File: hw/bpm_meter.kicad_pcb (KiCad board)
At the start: 2 copper layers, 55 x 73.5 mm, 103 parts, among them J1 Conn_01x03_Pin, J901 USB_C_Receptacle_USB2.0, Q1 AO3400A, Q10 DMN2004VK, Q11 DMN2004VK, Q12 DMN2004VK, Q13 DMN2004VK, Q2 DMN2004VK, Q3 DMN2004VK, Q4 DMN2004VK, Q5 DMN2004VK, Q6 DMN2004VK, Q7 DMN2004VK, Q8 DMN2004VK, Q9 DMN2004VK, SW901 SW_MEC_5E, U1 SLS0391FR1A1GD, U2 AOZ1282CI, U3 H11L1, U4 SLS0391FR1A1GD, U5 SLS0391FR1A1GD, U901 RP2040, U902 AMS1117-3.3, U903 W25Q128JVS, Y901 Crystal_GND24_Small

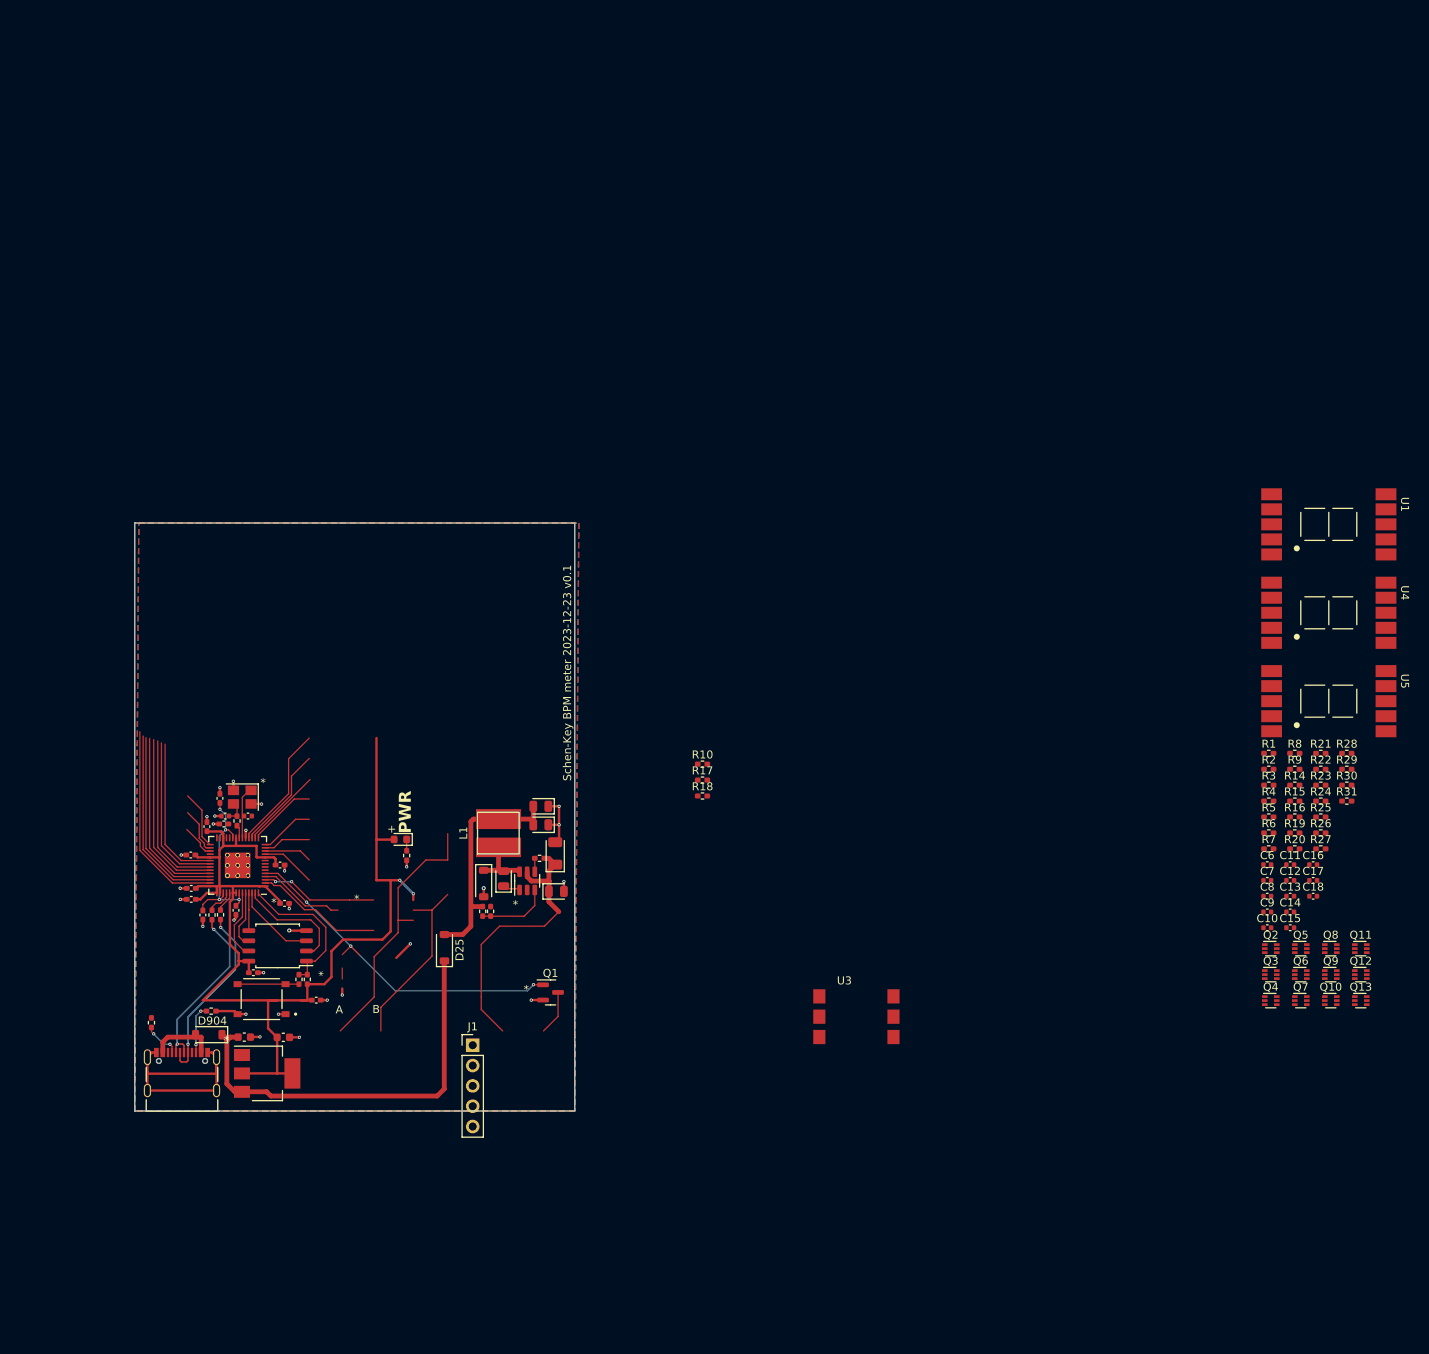
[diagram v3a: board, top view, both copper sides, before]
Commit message: Now using LP5030 LED driver
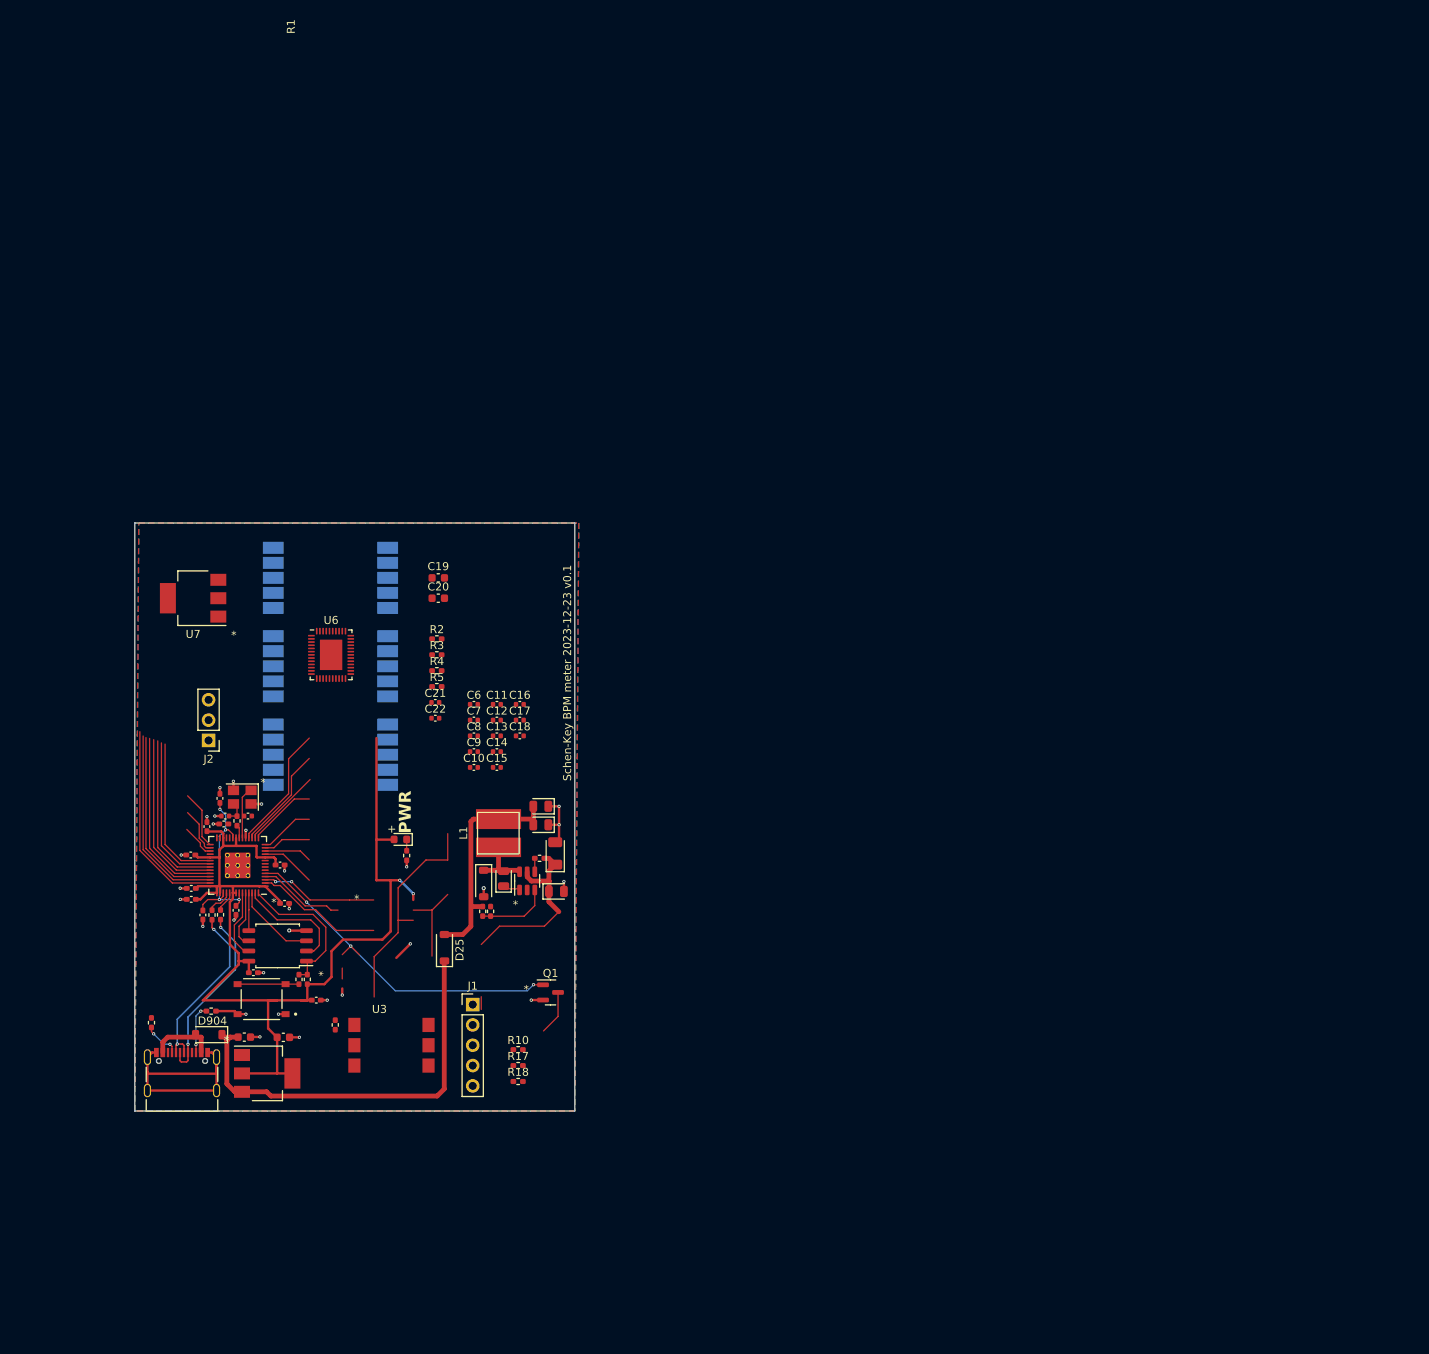
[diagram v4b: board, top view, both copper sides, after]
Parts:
- removed Q10, Q11, Q12, Q13, Q2, Q3, Q4, Q5, Q6, Q7, Q8, Q9: DMN2004VK, Package_TO_SOT_SMD:SOT-563
- removed R14, R15, R16, R19, R20, R21, R22, R23, R24, R25, R26, R27, R28, R29, R30, R31, R6, R7, R8, R9: 220, Resistor_SMD:R_0402_1005Metric_Pad0.72x0.64mm_HandSolder
- added C19: 10u, Capacitor_SMD:C_0603_1608Metric, F.Cu at (111.9, 65.9)
- added C20: 10u, Capacitor_SMD:C_0603_1608Metric, F.Cu at (111.9, 68.4)
- added C21: 1u, Capacitor_SMD:C_0402_1005Metric, F.Cu at (111.6, 81.4)
- added C22: 1u, Capacitor_SMD:C_0402_1005Metric, F.Cu at (111.6, 83.4)
- added J2: Conn_01x03_Pin, Connector_PinHeader_2.54mm:PinHeader_1x03_P2.54mm_Vertical, F.Cu at (83.2, 86.2)
- added U6: LP5030, Package_DFN_QFN:VQFN-46-1EP_5x6mm_P0.4mm_EP2.8x3.8mm, F.Cu at (98.5, 75.5)
- added U7: AMS1117-3.3, 00_project_library:SOT-223-3_TabPin2, F.Cu at (81.3, 68.4)
- J1: value Conn_01x03_Pin -> Conn_01x05_Pin
- R2, R3, R4, R5: value 220 -> 4k7
- U1, U4, U5: moved to B.Cu
- moved U1 125.0 mm to (98.5, 65.9), turned to 180 degrees
- moved U4 125.0 mm to (98.5, 76.9), turned to 180 degrees
- moved U5 125.0 mm to (98.5, 88.0), turned to 180 degrees
- moved R1 121.5 mm to (99.1, 121.7), turned to -90 degrees
- moved R2 105.3 mm to (111.8, 73.5)
- moved R3 105.3 mm to (111.8, 75.5)
- moved R4 105.3 mm to (111.8, 77.5)
- moved R5 105.3 mm to (111.8, 79.5)
- moved C10 101.2 mm to (116.4, 89.5)
- moved C12 101.2 mm to (119.3, 83.6)
- moved C13 101.2 mm to (119.3, 85.6)
- moved C14 101.2 mm to (119.3, 87.6)
- moved C15 101.2 mm to (119.3, 89.5)
- moved C16 101.2 mm to (122.1, 81.7)
- moved C17 101.2 mm to (122.1, 83.6)
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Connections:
- C11 pad 1: +5V -> +3.3VP
- C12 pad 1: +5V -> +3.3VP
- C13 pad 1: +5V -> +3.3VP
- C14 pad 1: +5V -> +3.3VP
- C15 pad 1: +5V -> +3.3VP
- C16 pad 1: +5V -> +3.3VP
- C17 pad 1: +5V -> +3.3VP
- C18 pad 1: +5V -> +3.3VP
- C6 pad 1: +5V -> +3.3VP
- C7 pad 1: +5V -> +3.3VP
- C8 pad 1: +5V -> +3.3VP
- C9 pad 1: +5V -> +3.3VP
- R2 pad 1: Net-(U1-A) -> Net-(U6-IREF)
- R2 pad 2: Net-(Q2-D1) -> GND
- R3 pad 1: Net-(U1-B) -> +3V3
- R3 pad 2: Net-(Q2-D2) -> scl
- R4 pad 1: Net-(U1-C) -> +3V3
- R4 pad 2: Net-(Q3-D1) -> sda
- R5 pad 1: Net-(U1-D) -> en
- R5 pad 2: Net-(Q3-D2) -> GND
- U1 pad 3: +5V -> +3.3VP
- U1 pad 8: +5V -> +3.3VP
- U4 pad 3: +5V -> +3.3VP
- U4 pad 8: +5V -> +3.3VP
- U5 pad 3: +5V -> +3.3VP
- U5 pad 8: +5V -> +3.3VP
- U901 pad 11: led_2A -> unconnected-(U901-GPIO8-Pad11)
- U901 pad 12: led_2B -> unconnected-(U901-GPIO9-Pad12)
- U901 pad 13: led_2C -> unconnected-(U901-GPIO10-Pad13)
- U901 pad 14: led_2D -> unconnected-(U901-GPIO11-Pad14)
- U901 pad 15: led_2E -> Net-(J2-Pin_1)
- U901 pad 16: led_2F -> Net-(J2-Pin_2)
- U901 pad 17: led_2G -> Net-(J2-Pin_3)
- U901 pad 18: led_2P -> unconnected-(U901-GPIO15-Pad18)
- U901 pad 2: led_1A -> sda
- U901 pad 27: led_3A -> unconnected-(U901-GPIO16-Pad27)
- U901 pad 28: led_3B -> unconnected-(U901-GPIO17-Pad28)
- U901 pad 29: led_3C -> unconnected-(U901-GPIO18-Pad29)
- U901 pad 3: led_1B -> scl
- U901 pad 30: led_3D -> unconnected-(U901-GPIO19-Pad30)
- U901 pad 31: led_3E -> unconnected-(U901-GPIO20-Pad31)
- U901 pad 32: led_3F -> unconnected-(U901-GPIO21-Pad32)
- U901 pad 34: led_3G -> unconnected-(U901-GPIO22-Pad34)
- U901 pad 35: led_3P -> unconnected-(U901-GPIO23-Pad35)
- U901 pad 4: led_1C -> en
- U901 pad 5: led_1D -> unconnected-(U901-GPIO3-Pad5)
- U901 pad 6: led_1E -> unconnected-(U901-GPIO4-Pad6)
- U901 pad 7: led_1F -> unconnected-(U901-GPIO5-Pad7)
- U901 pad 8: led_1G -> unconnected-(U901-GPIO6-Pad8)
- U901 pad 9: led_1P -> unconnected-(U901-GPIO7-Pad9)
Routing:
- net (no net): track 102.2 -> 39.9 mm
- net Net-(Q1-G): track 0.00 -> 44.2 mm, vias 0 -> 3
- net unconnected-(U901-GPIO23-Pad35): track 0.00 -> 19.9 mm
- net led_3P: track 19.9 -> 0.00 mm
- net unconnected-(U901-GPIO22-Pad34): track 0.00 -> 19.0 mm
- net led_3G: track 19.0 -> 0.00 mm
- net sda: track 0.00 -> 16.0 mm
- net led_1A: track 16.0 -> 0.00 mm
- net unconnected-(U901-GPIO15-Pad18): track 0.00 -> 15.6 mm
- net led_2P: track 15.6 -> 0.00 mm
- net scl: track 0.00 -> 14.6 mm, vias 0 -> 2
- net led_1B: track 14.6 -> 0.00 mm, vias 2 -> 0
- net led_2G: track 12.9 -> 0.00 mm
- net Net-(J2-Pin_3): track 0.00 -> 12.9 mm
- net led_1C: track 10.8 -> 0.00 mm
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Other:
- board text removed: "A"
- board text removed: "B"

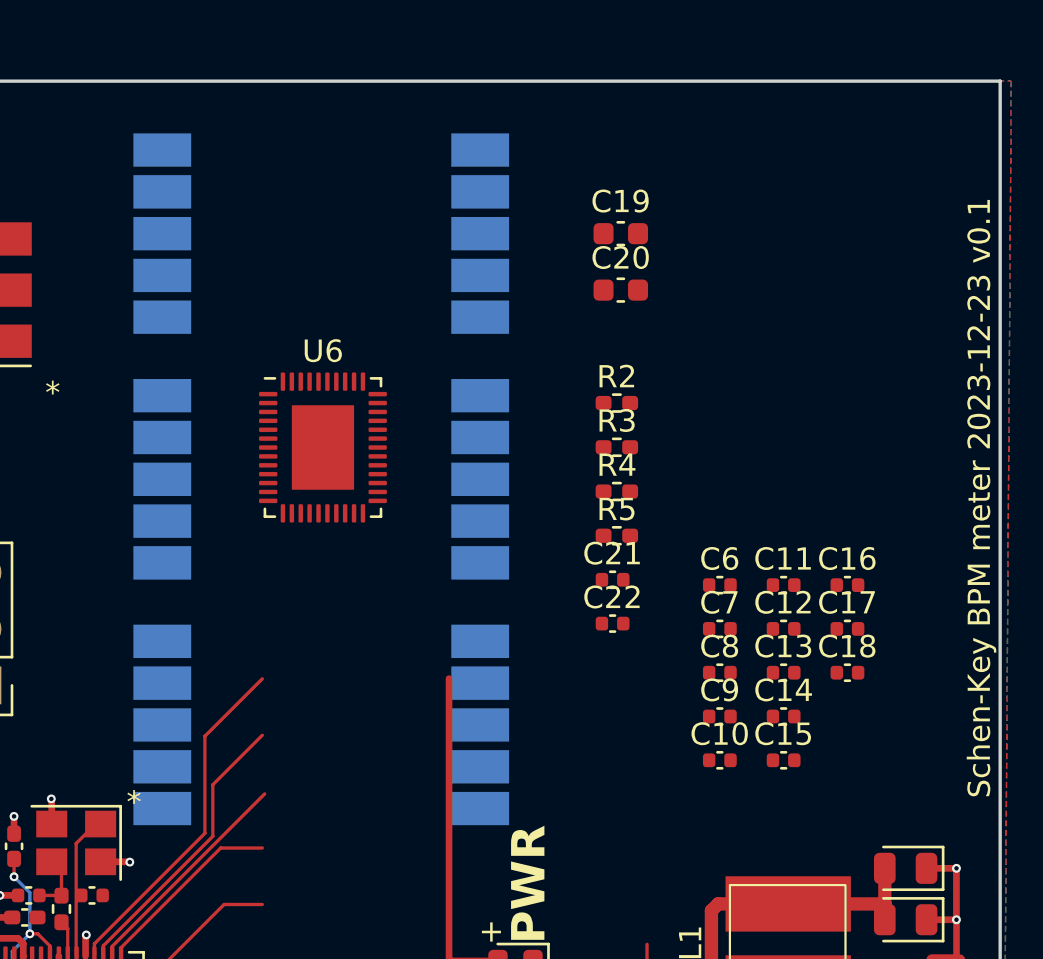
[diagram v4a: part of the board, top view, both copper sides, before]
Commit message: Changed LED driver to ISSI IS31FL3236A
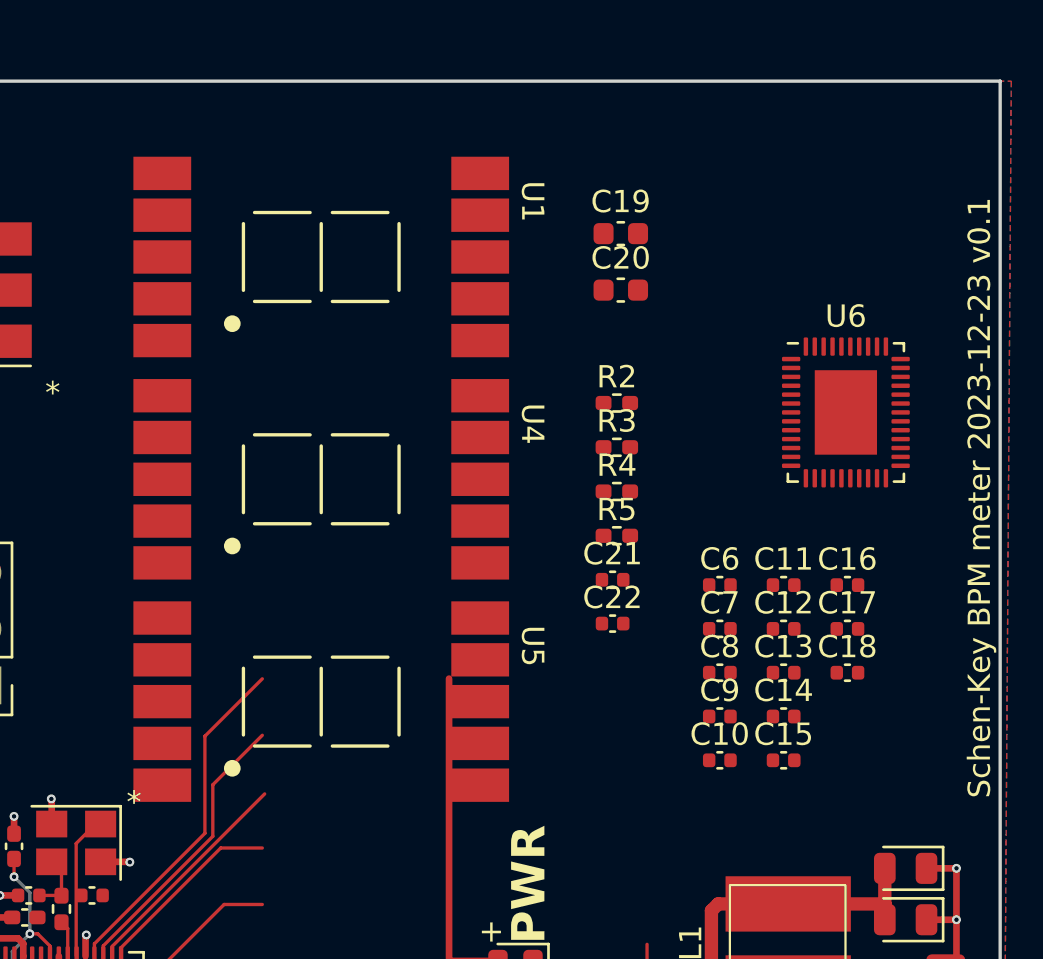
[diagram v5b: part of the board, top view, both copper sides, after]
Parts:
- U1, U4, U5: moved to F.Cu
- moved U6 23.6 mm to (122.1, 73.9)
- moved U1 1.05 mm to (98.5, 66.9), turned to 0 degrees
- moved U5 1.05 mm to (98.5, 86.9), turned to 0 degrees
- turned U4 to 0 degrees
